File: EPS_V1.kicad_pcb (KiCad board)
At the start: 2 copper layers, 82.5 x 82.5 mm, 197 parts, among them J1 Conn_01x19, J2 Conn_01x25, J3 Conn_01x9, J4 Conn_01x02, SW1 SWITCH, SW2 SWITCH, SW3 SWITCH, U1 MP2672AGD-0000-Z, U10 MP2672AGD-0000-Z, U11 MAX17205G+, U12 MP2672AGD-0000-Z, U13 MAX17205G+, U2 TPS62132RGTR, U3 TPS62133RGTR, U4 MP28167GQ-Z, U5 MAX17205G+, U6 TPS61088RHLR, U7 TPS2121RUXR, U8 MP2672AGD-0000-Z, U9 MAX17205G+

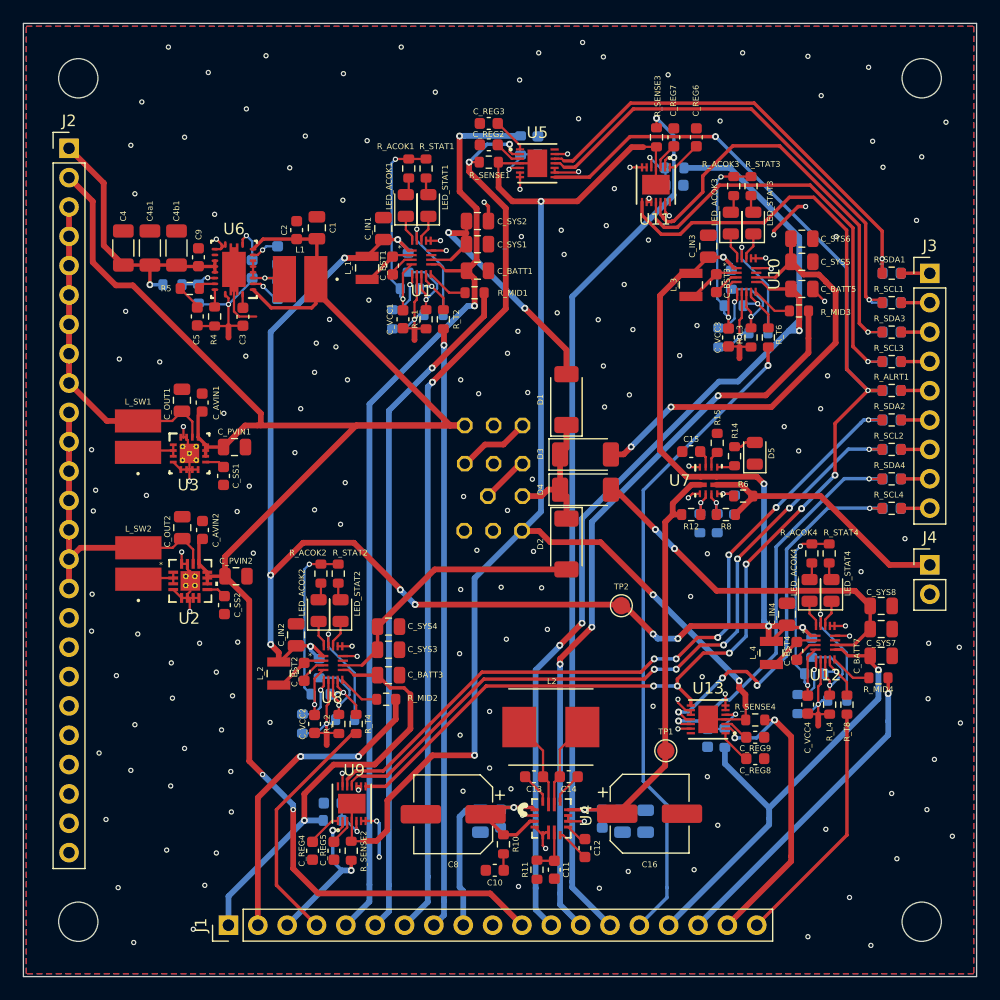
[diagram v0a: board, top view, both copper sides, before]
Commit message: Do layout with new regulator
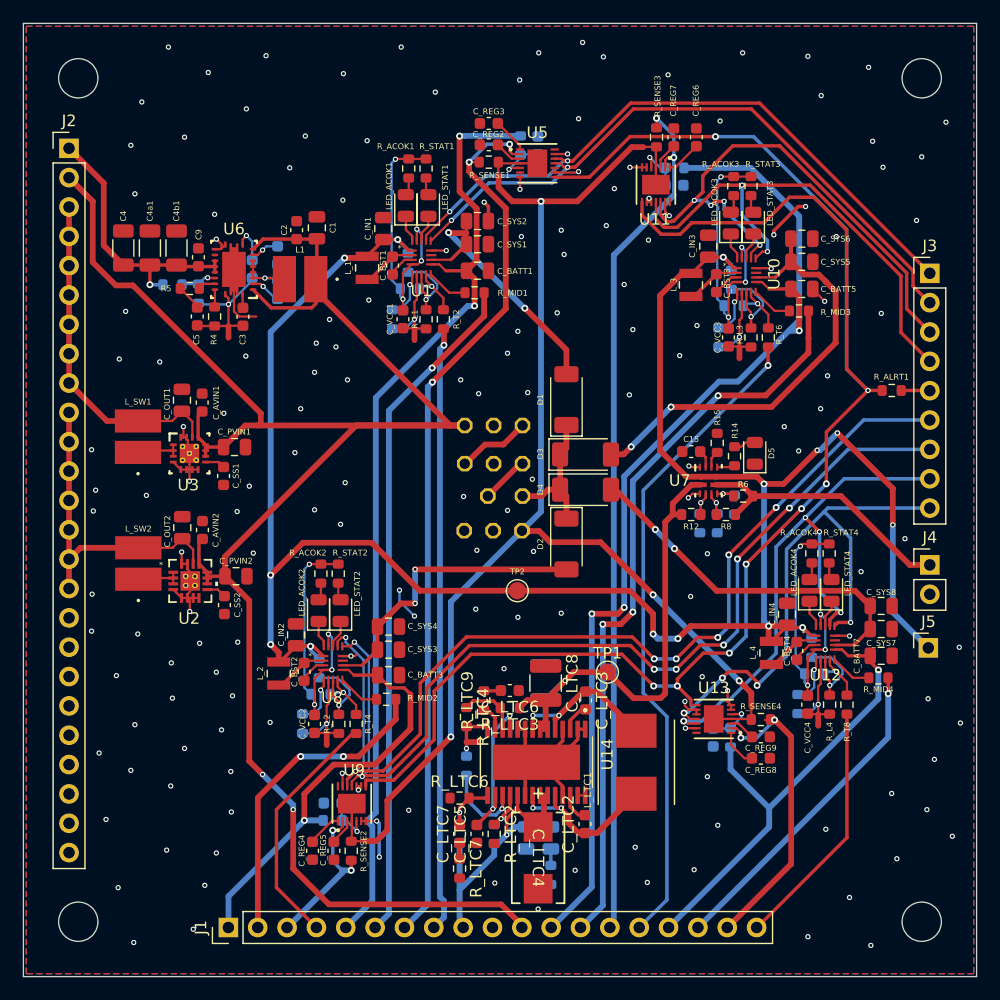
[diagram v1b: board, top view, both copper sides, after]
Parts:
- removed C10, C11: 22n, Capacitor_SMD:C_0603_1608Metric
- removed C12: 1u, Capacitor_SMD:C_0603_1608Metric
- removed C13, C14, C1A1, C2A1: 100n, Capacitor_SMD:C_0603_1608Metric
- removed C16, C8: 100u, Capacitor_SMD:CP_Elec_6.3x5.4
- removed C1B1: 22u, Capacitor_SMD:C_0805_2012Metric
- removed C2B1, C2C1: 10u, Capacitor_SMD:C_0805_2012Metric
- removed D_ALRT1, D_SCL1, D_SCL2, D_SCL3, D_SCL4, D_SDA1, D_SDA2, D_SDA3, D_SDA4: 4.7, Diode_SMD:D_0603_1608Metric
- removed L2: 4.7u, footprints:IND_ASPI-7318-4R7M-T
- removed R10: 499k, Resistor_SMD:R_0603_1608Metric
- removed R11: 21.5k, Resistor_SMD:R_0603_1608Metric
- removed R_SCL1, R_SCL2, R_SCL3, R_SCL4, R_SDA1, R_SDA2, R_SDA3, R_SDA4: 150R, Resistor_SMD:R_0603_1608Metric
- removed R_VBATT1, R_VBATT2, R_VBATT3, R_VBATT4: 33k, Resistor_SMD:R_0603_1608Metric
- removed U4: MP28167GQ-Z, footprints:QFN-16_MP28167GQ_MNP
- added C_LTC1: 10u, Capacitor_SMD:C_0805_2012Metric, B.Cu at (102.2, 129.2)
- added C_LTC10: 10u, Capacitor_SMD:C_0805_2012Metric, B.Cu at (104.4, 129.2)
- added C_LTC2: 100n, Capacitor_SMD:C_0603_1608Metric, F.Cu at (107.3, 128.1)
- added C_LTC3: 100n, Capacitor_SMD:C_0603_1608Metric, F.Cu at (107.4, 117.3)
- added C_LTC4: 220u, footprints:CAPMP7.6X4.3_4.3N_KEM, F.Cu at (103.3, 131.0)
- added C_LTC5: 4.7u, Capacitor_SMD:C_0603_1608Metric, F.Cu at (98.0, 128.9)
- added C_LTC6: 560p, Capacitor_SMD:C_0603_1608Metric, F.Cu at (100.8, 116.5)
- added C_LTC7: 4.7n, Capacitor_SMD:C_0603_1608Metric, F.Cu at (96.5, 128.9)
- added C_LTC8: 100u, Capacitor_SMD:C_1210_3225Metric, F.Cu at (104.0, 115.8)
- added C_LTC9: 100u, Capacitor_SMD:C_1210_3225Metric, B.Cu at (104.0, 115.8)
- added J5: Conn_01x01, Connector_PinHeader_2.54mm:PinHeader_1x01_P2.54mm_Horizontal, F.Cu at (137.1, 112.8)
- added L_LTC1: 4.7u, footprints:IND_ASPI-7318-4R7M-T, F.Cu at (111.8, 122.7)
- added NT11: NetTie_2, NetTie:NetTie-2_SMD_Pad0.5mm, F.Cu at (97.6, 121.0)
- added R_LTC1: 199k, Resistor_SMD:R_0603_1608Metric, B.Cu at (99.5, 128.9)
- added R_LTC10: 0.33R, Resistor_SMD:R_0603_1608Metric, B.Cu at (104.4, 132.4)
- added R_LTC2: 100k, Resistor_SMD:R_0603_1608Metric, F.Cu at (99.5, 128.9)
- added R_LTC3: 536k, Resistor_SMD:R_0603_1608Metric, F.Cu at (100.8, 118.0)
- added R_LTC4: 102k, Resistor_SMD:R_0603_1608Metric, F.Cu at (97.1, 118.8)
- added R_LTC5: R5, Resistor_SMD:R_0603_1608Metric, B.Cu at (96.5, 128.9)
- added R_LTC6: 100k, Resistor_SMD:R_0603_1608Metric, F.Cu at (96.5, 125.8)
- added R_LTC7: 7.5k, Resistor_SMD:R_0603_1608Metric, F.Cu at (96.5, 131.9)
- added R_LTC8: 162k, Resistor_SMD:R_0603_1608Metric, B.Cu at (97.1, 123.0)
- added R_LTC9: 100k, Resistor_SMD:R_0603_1608Metric, F.Cu at (98.6, 117.3)
- added U14: LTC3119EFE_PBF, footprints:SOP65P640X120-29N, F.Cu at (103.2, 122.7)
- moved TP2 9.09 mm to (101.5, 107.8)
- moved TP1 8.47 mm to (109.3, 114.9)
- moved NT9 0.51 mm to (121.8, 117.3)
- moved C_BATT8 0.49 mm to (118.5, 120.6)
- moved R_BATT4 0.49 mm to (120.0, 120.6)
- moved C_REG8 0.49 mm to (122.6, 122.4)
- moved C_REG9 0.49 mm to (122.6, 120.5)
- moved R_SENSE4 0.49 mm to (122.6, 119.0)
- moved U13 0.49 mm to (118.5, 119.0)
- moved J1 0.20 mm to (76.5, 137.0)
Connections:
- C_VCC1 pad 2: Net-(U1-VCC) -> Net-(U1-CV)
- C_VCC2 pad 2: Net-(U8-VCC) -> Net-(U8-CV)
- C_VCC3 pad 2: Net-(U10-VCC) -> Net-(U10-CV)
- C_VCC4 pad 2: Net-(U12-VCC) -> Net-(U12-CV)
- R_ACOK1 pad 2: Net-(U1-VCC) -> Net-(U1-CV)
- R_ACOK2 pad 2: Net-(U8-VCC) -> Net-(U8-CV)
- R_ACOK3 pad 2: Net-(U10-VCC) -> Net-(U10-CV)
- R_ACOK4 pad 2: Net-(U12-VCC) -> Net-(U12-CV)
- R_STAT1 pad 1: Net-(U1-VCC) -> Net-(U1-CV)
- R_STAT2 pad 1: Net-(U8-VCC) -> Net-(U8-CV)
- R_STAT3 pad 1: Net-(U10-VCC) -> Net-(U10-CV)
- R_STAT4 pad 1: Net-(U12-VCC) -> Net-(U12-CV)
- R_T1 pad 1: Net-(U1-VCC) -> Net-(U1-CV)
- R_T3 pad 1: Net-(U8-VCC) -> Net-(U8-CV)
- R_T5 pad 1: Net-(U10-VCC) -> Net-(U10-CV)
- R_T7 pad 1: Net-(U12-VCC) -> Net-(U12-CV)
- U1 pad 14: GND -> I2C1_SCL
- U1 pad 15: GND -> I2C1_SDA
- U1 pad 4: Net-(U1-VCC) -> Net-(U1-CV)
- U10 pad 14: GND -> I2C3_SCL
- U10 pad 15: GND -> I2C3_SDA
- U10 pad 4: Net-(U10-VCC) -> Net-(U10-CV)
- U11 pad 11: Net-(D_SCL3-K) -> I2C3_SCL
- U11 pad 12: Net-(D_SDA3-K) -> I2C3_SDA
- U12 pad 14: GND -> I2C4_SCL
- U12 pad 15: GND -> I2C4_SDA
- U12 pad 4: Net-(U12-VCC) -> Net-(U12-CV)
- U13 pad 11: Net-(D_SCL4-K) -> I2C4_SCL
- U13 pad 12: Net-(D_SDA4-K) -> I2C4_SDA
- U2 pad V: (no net) -> GND
- U3 pad 18: (no net) -> GND
- U3 pad 19: (no net) -> GND
- U3 pad 20: (no net) -> GND
- U3 pad 21: (no net) -> GND
- U3 pad 22: (no net) -> GND
- U5 pad 11: Net-(D_SCL1-K) -> I2C1_SCL
- U5 pad 12: Net-(D_SDA1-K) -> I2C1_SDA
- U8 pad 14: GND -> I2C2_SCL
- U8 pad 15: GND -> I2C2_SDA
- U8 pad 4: Net-(U8-VCC) -> Net-(U8-CV)
- U9 pad 11: Net-(D_SCL2-K) -> I2C2_SCL
- U9 pad 12: Net-(D_SDA2-K) -> I2C2_SDA
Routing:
- net I2C2_SDA: track 2.48 -> 85.5 mm, vias 0 -> 7
- net I2C2_SCL: track 2.47 -> 83.8 mm, vias 0 -> 7
- net Net-(D_SDA2-K): track 64.6 -> 0.00 mm, vias 6 -> 0
- net Net-(D_SCL2-K): track 63.1 -> 0.00 mm, vias 6 -> 0
- net I2C1_SCL: track 2.47 -> 57.0 mm, vias 0 -> 2
- net I2C1_SDA: track 2.48 -> 56.3 mm, vias 0 -> 2
- net I2C4_SCL: track 2.48 -> 48.6 mm, vias 0 -> 4
- net I2C4_SDA: track 2.48 -> 47.8 mm, vias 0 -> 4
- net I2C3_SDA: track 2.48 -> 46.4 mm, vias 0 -> 4
- net Net-(D_SCL1-K): track 42.5 -> 0.00 mm, vias 1 -> 0
- net I2C3_SCL: track 2.48 -> 44.1 mm, vias 0 -> 2
- net Net-(D_SDA1-K): track 40.1 -> 0.00 mm, vias 1 -> 0
- net Net-(D_SDA3-K): track 37.0 -> 0.00 mm, vias 1 -> 0
- net Net-(D_SCL3-K): track 36.5 -> 0.00 mm, vias 1 -> 0
- net Net-(D_SDA4-K): track 34.1 -> 0.00 mm, vias 2 -> 0
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
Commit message: fix U6 EN pin, add ALRT pullup R, update 3dmodels, regen step
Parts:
- added R10: 10k, Resistor_SMD:R_0603_1608Metric, F.Cu at (82.8, 84.2)
- added R11: 15k, Resistor_SMD:R_0603_1608Metric, F.Cu at (80.4, 85.0)
- added R_ALRT2: 10k, Resistor_SMD:R_0603_1608Metric, F.Cu at (67.0, 100.0)
- R_ISET1, R_ISET2, R_ISET3, R_ISET4: value 6k -> 24k
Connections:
- U2 pad V: GND -> (no net)
- U3 pad 18: GND -> (no net)
- U3 pad 19: GND -> (no net)
- U3 pad 20: GND -> (no net)
- U3 pad 21: GND -> (no net)
- U3 pad 22: GND -> (no net)
- U6 pad 2: CHG_OUT -> Net-(U6-EN)
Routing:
- net ALRT: track 154.2 -> 224.2 mm, vias 8 -> 9
- net CHG_OUT: track 174.6 -> 169.7 mm
- net Net-(U6-EN): track 0.00 -> 4.71 mm
- net +3V3: track 28.3 -> 31.8 mm
- net GND: vias 169 -> 189

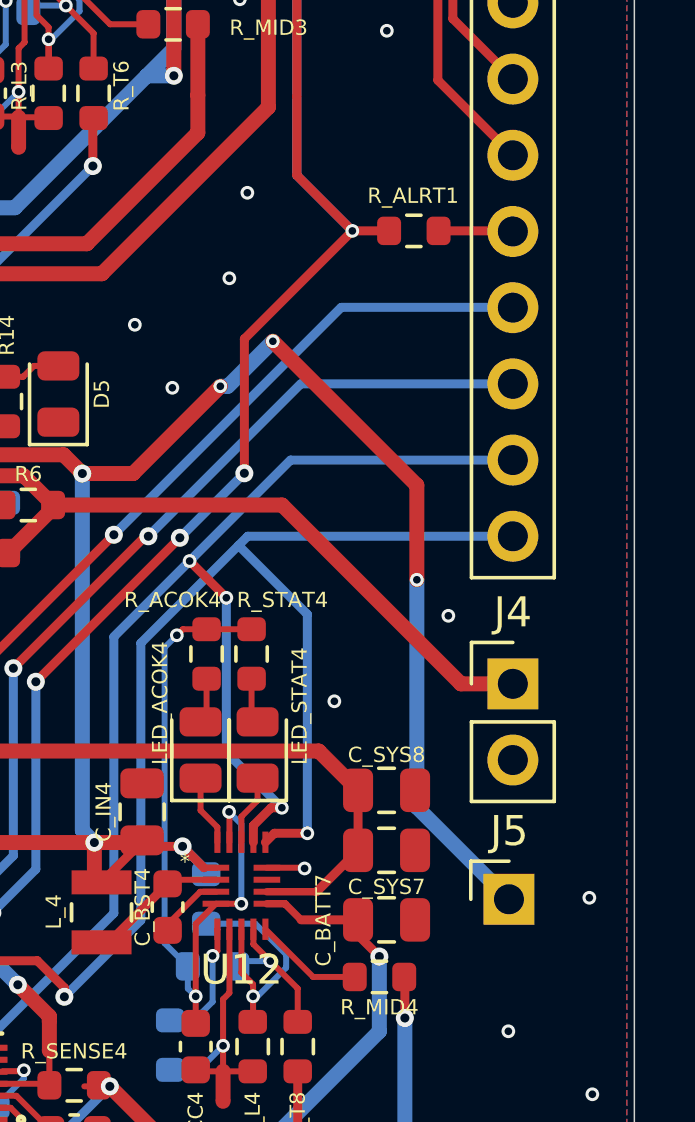
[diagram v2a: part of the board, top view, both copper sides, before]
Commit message: Remove extra ALRT resistor
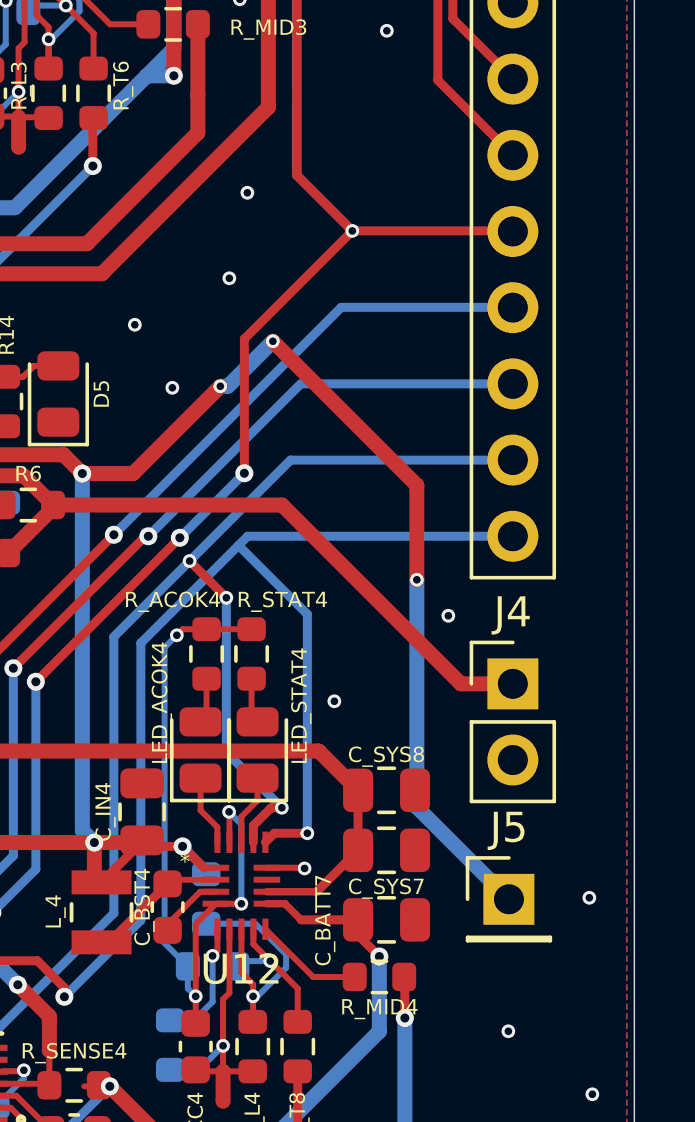
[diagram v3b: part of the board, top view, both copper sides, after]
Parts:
- removed R_ALRT1: 1k, Resistor_SMD:R_0603_1608Metric
- J5: footprint Connector_PinHeader_2.54mm:PinHeader_1x01_P2.54mm_Horizontal -> Connector_PinHeader_2.54mm:PinHeader_1x01_P2.54mm_Vertical
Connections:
- J3 pad 5: Net-(J3-Pin_5) -> ALRT
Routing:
- net ALRT: track 224.2 -> 228.3 mm
- net Net-(J3-Pin_5): track 2.48 -> 0.00 mm
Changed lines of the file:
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@@
 		)
 	)
-	(footprint "Connector_PinHeader_2.54mm:PinHeader_1x01_P2.54mm_Horizontal"
+	(footprint "Connector_PinHeader_2.54mm:PinHeader_1x01_P2.54mm_Vertical"
 		(layer "F.Cu")
 		(at 137.07 112.8)
-		(descr "Through hole angled pin header, 1x01, 2.54mm pitch, 6mm pin length, single row")
-		(tags "Through hole angled pin header THT 1x01 2.54mm single row")
+		(descr "Through hole straight pin header, 1x01, 2.54mm pitch, single row")
+		(tags "Through hole pin header THT 1x01 2.54mm single row")
 		(property "Reference" "J5"
-			(at 0.01 -2.27 0)
+			(at 0 -2.38 0)
 			(layer "F.SilkS")
 			(effects
@@
 		)
 		(property "Value" "Conn_01x01"
-			(at 4.385 2.27 0)
+			(at 0 2.38 0)
 			(layer "F.Fab")
 			(effects
@@
 			)
 		)
-		(attr through_hole dnp)
+		(attr through_hole)
 		(duplicate_pad_numbers_are_jumpers no)
 		(fp_line
-			(start -1.27 -1.27)
-			(end 0 -1.27)
+			(start -1.38 -1.38)
+			(end 0 -1.38)
+			(stroke
+				(width 0.12)
+				(type solid)
+			)
+			(layer "F.SilkS")
+		)
+		(fp_line
+			(start -1.38 0)
+			(end -1.38 -1.38)
+			(stroke
+				(width 0.12)
+				(type solid)
+			)
+			(layer "F.SilkS")
+		)
+		(fp_line
+			(start -1.38 1.27)
+			(end -1.38 1.38)
+			(stroke
+				(width 0.12)
+				(type solid)
+			)
+			(layer "F.SilkS")
+		)
+		(fp_line
+			(start -1.38 1.27)
+			(end 1.38 1.27)
+			(stroke
+				(width 0.12)
+				(type solid)
+			)
+			(layer "F.SilkS")
+		)
+		(fp_line
+			(start -1.38 1.38)
+			(end 1.38 1.38)
 			(stroke
 				(width 0.12)
@@
 		)
 		(fp_line
-			(start -1.27 0)
-			(end -1.27 -1.27)
+			(start 1.38 1.27)
+			(end 1.38 1.38)
 			(stroke
 				(width 0.12)
@@
 		(fp_rect
 			(start -1.77 -1.77)
-			(end 2.03 1.77)
+			(end 1.77 1.77)
 			(stroke
 				(width 0.05)
@@
 		)
 		(fp_line
-			(start -0.32 -0.32)
-			(end -0.32 0.32)
+			(start -1.27 -0.635)
+			(end -0.635 -1.27)
 			(stroke
 				(width 0.1)
@@
 		)
 		(fp_line
-			(start -0.32 -0.32)
-			(end 1.5 -0.32)
+			(start -1.27 1.27)
+			(end -1.27 -0.635)
+			(stroke
+				(width 0.1)
+				(type solid)
+			)
+			(layer "F.Fab")
+		)
+		(fp_line
+			(start -0.635 -1.27)
+			(end 1.27 -1.27)
+			(stroke
+				(width 0.1)
+				(type solid)
+			)
+			(layer "F.Fab")
+		)
+		(fp_line
+			(start 1.27 -1.27)
+			(end 1.27 1.27)
 			(stroke
 				(width 0.1)
@@
 		)
 		(fp_line
-			(start -0.32 0.32)
-			(end 1.5 0.32)
+			(start 1.27 1.27)
+			(end -1.27 1.27)
 			(stroke
 				(width 0.1)
@@
 		)
 		(fp_text user "${REFERENCE}"
-			(at 2.77 0 90)
+			(at 0 0 90)
 			(layer "F.Fab")
 			(effects
@@
 		)
 		(embedded_fonts no)
-		(model "kicad-embed://PinHeader_1x01_P2.54mm_Horizontal.step"
+		(model "${KICAD10_3DMODEL_DIR}/Connector_PinHeader_2.54mm.3dshapes/PinHeader_1x01_P2.54mm_Vertical.step"
 			(offset
 				(xyz 0 0 0)
@@
 		)
 	)
-	(footprint "Resistor_SMD:R_0603_1608Metric"
-		(layer "F.Cu")
-		(at 133.9 90.52)
-		(descr "Resistor SMD 0603 (1608 Metric), square (rectangular) end terminal, IPC-7351 nominal, (Body size source: IPC-SM-782 page 72, https://www.pcb-3d.com/wordpress/wp-content/uploads/ipc-sm-782a_amendment_1_and_2.pdf)")
-		(tags "resistor")
-		(property "Reference" "R_ALRT1"
-			(at -1.55 -1.17 0)
-			(layer "F.SilkS")
-			(effects
-				(font
-					(size 0.508 0.508)
-					(thickness 0.127)
-				)
-				(justify left)
-			)
-		)
-		(property "Value" "1k"
-			(at 0 1.43 0)
-			(layer "F.Fab")
-			(effects
-				(font
-					(size 1 1)
-					(thickness 0.15)
-				)
-			)
-		)
-		(property "Datasheet" ""
-			(at 0 0 0)
-			(layer "F.Fab")
-			(hide yes)
-			(effects
-				(font
-					(size 1.27 1.27)
-				)
-			)
-		)
-		(property "Description" "Resistor, US symbol"
-			(at 0 0 0)
-			(layer "F.Fab")
-			(hide yes)
-			(effects
-				(font
-					(size 1.27 1.27)
-				)
-			)
-		)
-		(property "KiLib_Generator" "SMD_2terminal_chip_molded"
-			(at 0 0 0)
-			(layer "F.SilkS")
-			(hide yes)
-			(effects
-				(font
-					(size 1 1)
-					(thickness 0.15)
-				)
-			)
-		)
-		(property ki_fp_filters "R_*")
-		(sheetname "/Connectors/")
-		(sheetfile "schematics/EPS_V1_connectors.kicad_sch")
-		(units
-			(unit
-				(name "A")
-				(pins "1" "2")
-			)
-		)
-		(attr smd)
-		(duplicate_pad_numbers_are_jumpers no)
-		(fp_line
-			(start -0.237258 -0.5225)
-			(end 0.237258 -0.5225)
-			(stroke
-				(width 0.12)
-				(type solid)
-			)
-			(layer "F.SilkS")
-		)
-		(fp_line
-			(start -0.237258 0.5225)
-			(end 0.237258 0.5225)
-			(stroke
-				(width 0.12)
-				(type solid)
-			)
-			(layer "F.SilkS")
-		)
-		(fp_rect
-			(start -1.48 -0.73)
-			(end 1.48 0.73)
-			(stroke
-				(width 0.05)
-				(type solid)
-			)
-			(fill no)
-			(layer "F.CrtYd")
-		)
-		(fp_rect
-			(start -0.8 -0.4125)
-			(end 0.8 0.4125)
-			(stroke
-				(width 0.1)
-				(type solid)
-			)
-			(fill no)
-			(layer "F.Fab")
-		)
-		(fp_text user "${REFERENCE}"
-			(at 0 0 0)
-			(layer "F.Fab")
-			(effects
-				(font
-					(size 0.4 0.4)
-					(thickness 0.06)
-				)
-			)
-		)
-		(pad "1" smd roundrect
-			(at -0.825 0)
-			(size 0.8 0.95)
-			(layers "F.Cu" "F.Mask" "F.Paste")
-			(roundrect_rratio 0.25)
-			(net "ALRT")
-			(pintype "passive")
-		)
-		(pad "2" smd roundrect
-			(at 0.825 0)
-			(size 0.8 0.95)
-			(layers "F.Cu" "F.Mask" "F.Paste")
-			(roundrect_rratio 0.25)
-			(net "Net-(J3-Pin_5)")
-			(pintype "passive")
-		)
-		(embedded_fonts no)
-		(model "kicad-embed://R_0603_1608Metric.step"
-			(offset
-				(xyz 0 0 0)
-			)
-			(scale
-				(xyz 1 1 1)
-			)
-			(rotate
-				(xyz 0 0 0)
-			)
-		)
-	)
 	(footprint "TestPoint:TestPoint_Pad_D1.5mm"
 		(layer "F.Cu")
@@
 			(layers "*.Cu" "*.Mask")
 			(remove_unused_layers no)
-			(net "Net-(J3-Pin_5)")
+			(net "ALRT")
 			(pinfunction "Pin_5_5")
 			(pintype "passive")
@@
 	)
 	(segment
+		(start 131.851142 90.52)
+		(end 137.18 90.52)
+		(width 0.3)
+		(layer "F.Cu")
+		(net "ALRT")
+	)
+	(segment
 		(start 116.516962 117.266962)
 		(end 116.516962 117.786296)
@@
 	)
 	(segment
-		(start 131.851142 90.52)
-		(end 131.849938 90.521204)
-		(width 0.3)
-		(layer "F.Cu")
-		(net "ALRT")
-	)
-	(segment
 		(start 125.05 73.8)
 		(end 122.85 76)
@@
 	)
 	(segment
-		(start 133.075 90.52)
+		(start 131.849938 90.521204)
 		(end 131.851142 90.52)
 		(width 0.3)
@@
 	)
 	(segment
-		(start 107.741203 72.058797)
-		(end 111.25 68.55)
+		(start 137.18 90.52)
+		(end 137.2 90.54)
 		(width 0.3)
 		(layer "F.Cu")
@@
 	)
 	(segment
-		(start 133.075 90.546142)
-		(end 133.075 90.52)
+		(start 107.741203 72.058797)
+		(end 111.25 68.55)
 		(width 0.3)
 		(layer "F.Cu")
@@
 	)
 	(segment
-		(start 137.18 90.52)
-		(end 137.2 90.54)
-		(width 0.3)
-		(layer "F.Cu")
-		(net "Net-(J3-Pin_5)")
-	)
-	(segment
-		(start 134.725 90.52)
-		(end 137.18 90.52)
-		(width 0.3)
-		(layer "F.Cu")
-		(net "Net-(J3-Pin_5)")
-	)
-	(segment
